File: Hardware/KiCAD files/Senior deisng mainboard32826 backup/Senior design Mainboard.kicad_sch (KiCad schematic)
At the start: 0 parts

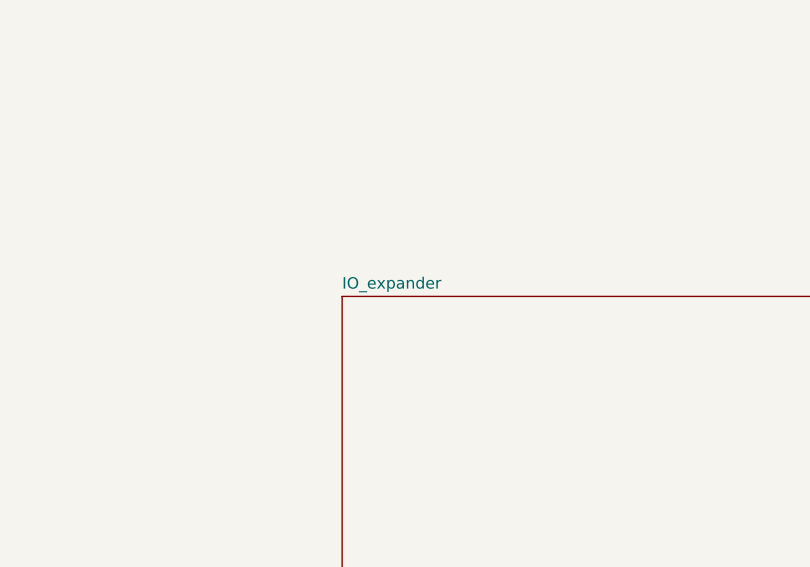
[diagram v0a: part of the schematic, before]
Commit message: IO pull resistors, Motor driver V1, LCD communication
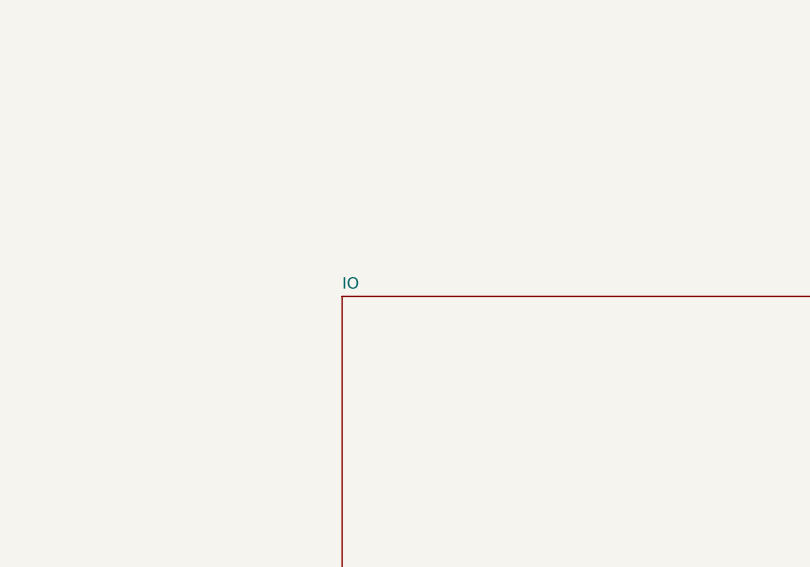
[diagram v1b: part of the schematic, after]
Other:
- sheet IO_expander renamed IO
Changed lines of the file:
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@@
 			(color 0 0 0 0)
 		)
-		(property "Sheetname" "IO_expander"
+		(property "Sheetname" "IO"
 			(at 669.925 936.5484 0)
 			(show_name no)
